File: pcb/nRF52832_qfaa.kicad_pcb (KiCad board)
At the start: 4 copper layers, 40 x 20 mm, 131 parts, among them J1 Conn_01x01_Female, J3 USB_B_Micro, J4 Conn_01x02_Socket, J5 Conn_01x03_Socket, Q1 PMOS, U2 W25Q128JWPIQ, U3 TPS63802DLAR, U4 BQ24078RGTR, U5 RV-4162-C7, U6 SN74LVC1G79DBVT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

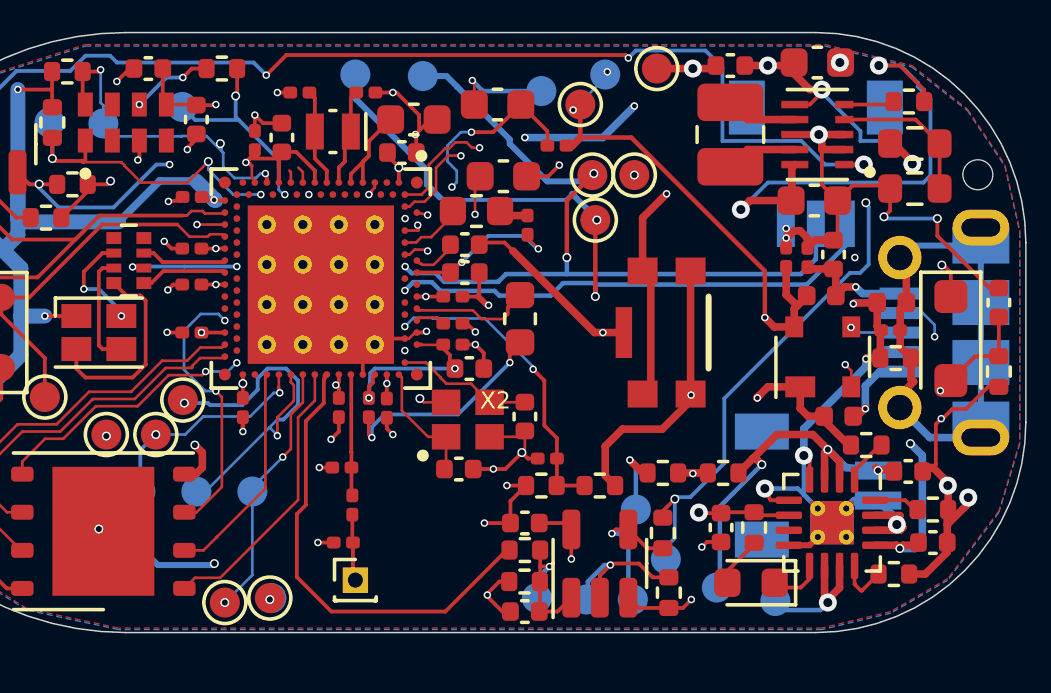
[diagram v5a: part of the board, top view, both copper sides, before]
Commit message: fixed couple issues with DF 1.4 (FF_CLK not propagated, RTC_INTR output inverted)
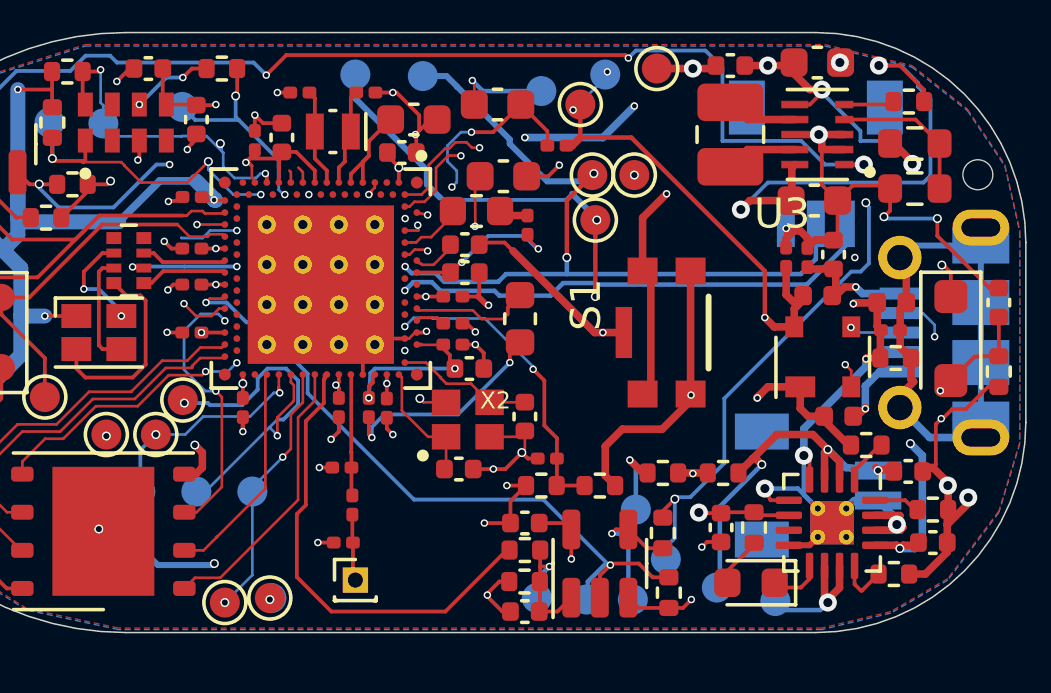
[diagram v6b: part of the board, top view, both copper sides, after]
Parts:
- added G***: LOGO, _other:df_symbol, B.Cu at (122.2, 99.2)
- R10, R11: value 100K -> 1M
- R15: value 511k -> 255k
- moved FB1 0.12 mm to (148.1, 97.8)
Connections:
- U7 pad AL19: unconnected-(U7D-P1.04-PadAL19) -> FF_CLK
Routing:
- net FF_CLK: track 5.17 -> 23.6 mm, vias 1 -> 2
- net unconnected-(U7C-P0.14/IO[1]-PadAK8): track 0.00 -> 1.96 mm, vias 0 -> 1
- net unconnected-(U7D-P1.06-PadAL21): track 0.00 -> 1.66 mm, vias 0 -> 1
- net VCC: track 132.8 -> 132.3 mm
- net GND: vias 59 -> 58
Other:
- board text removed: "Dictofun 1.3"
- board text removed: "github.com/rundb/dictofun"
